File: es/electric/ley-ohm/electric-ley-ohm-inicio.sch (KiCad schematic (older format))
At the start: 60 parts

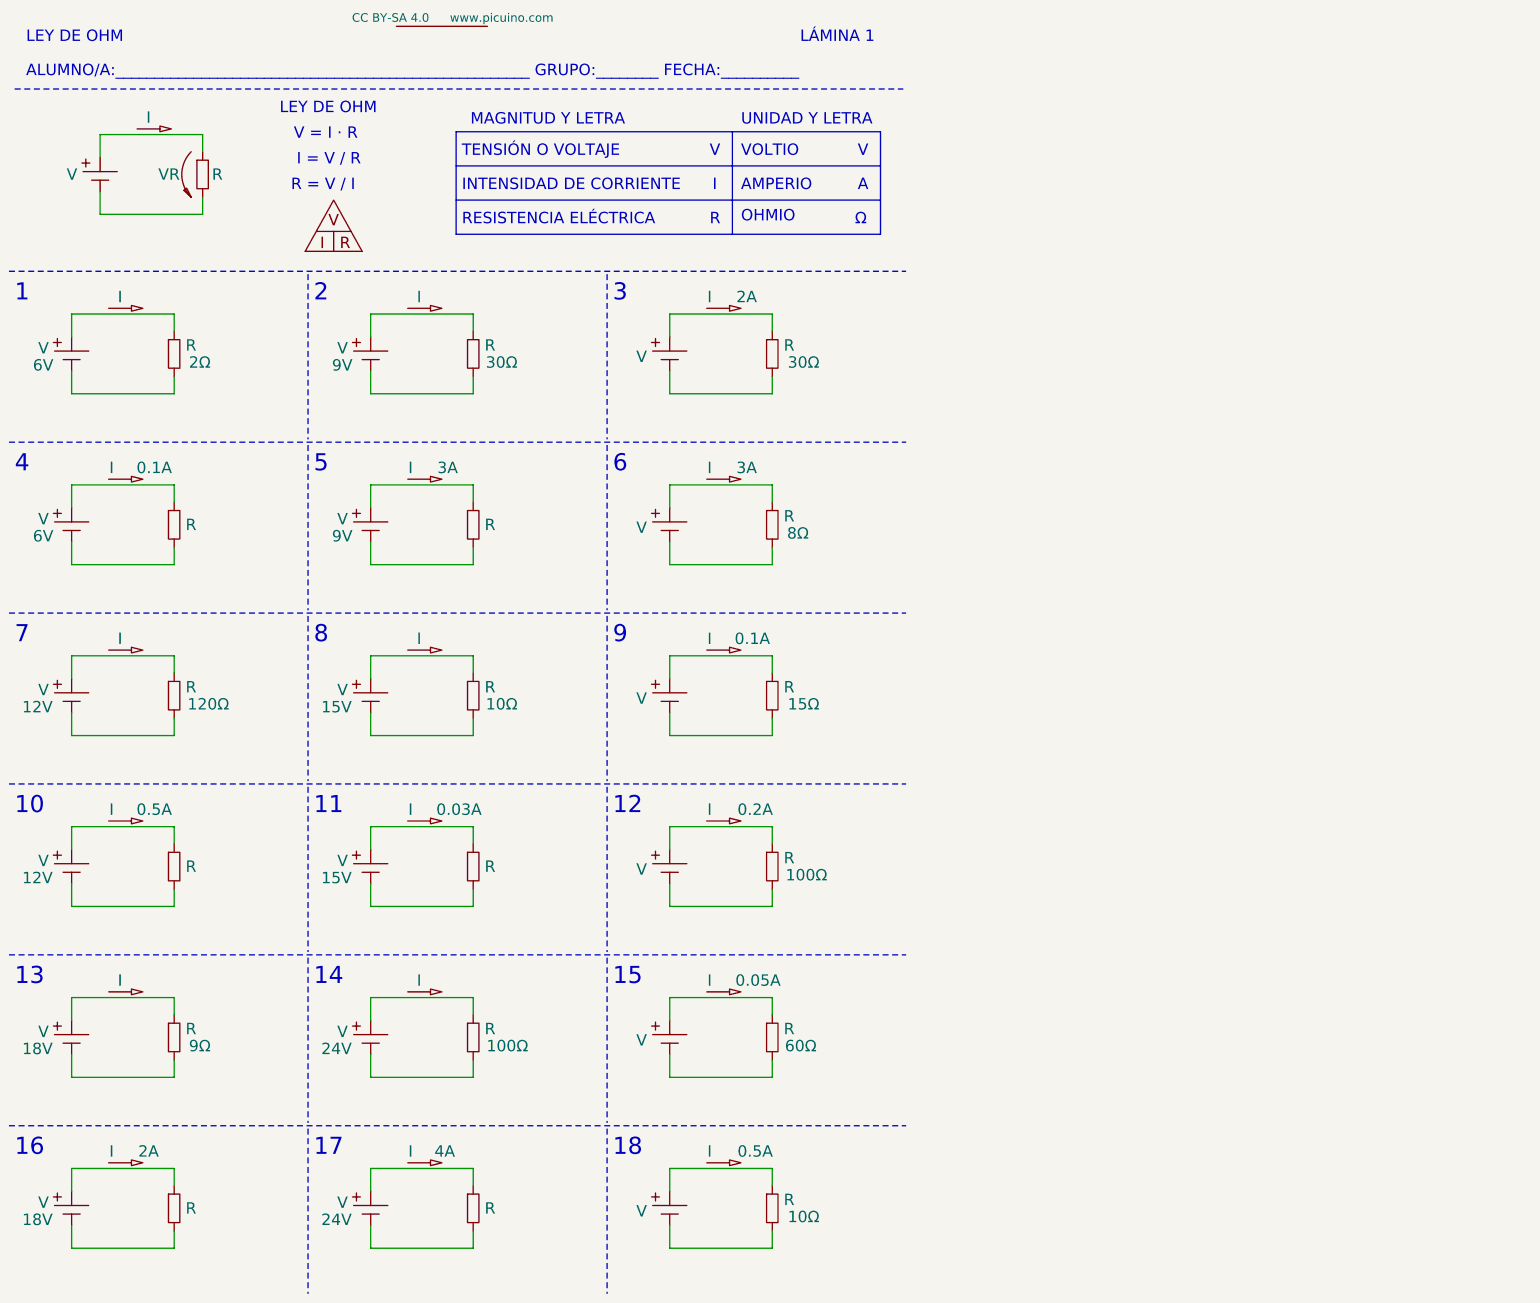
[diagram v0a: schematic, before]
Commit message: Añadida página de la ley de Ohm
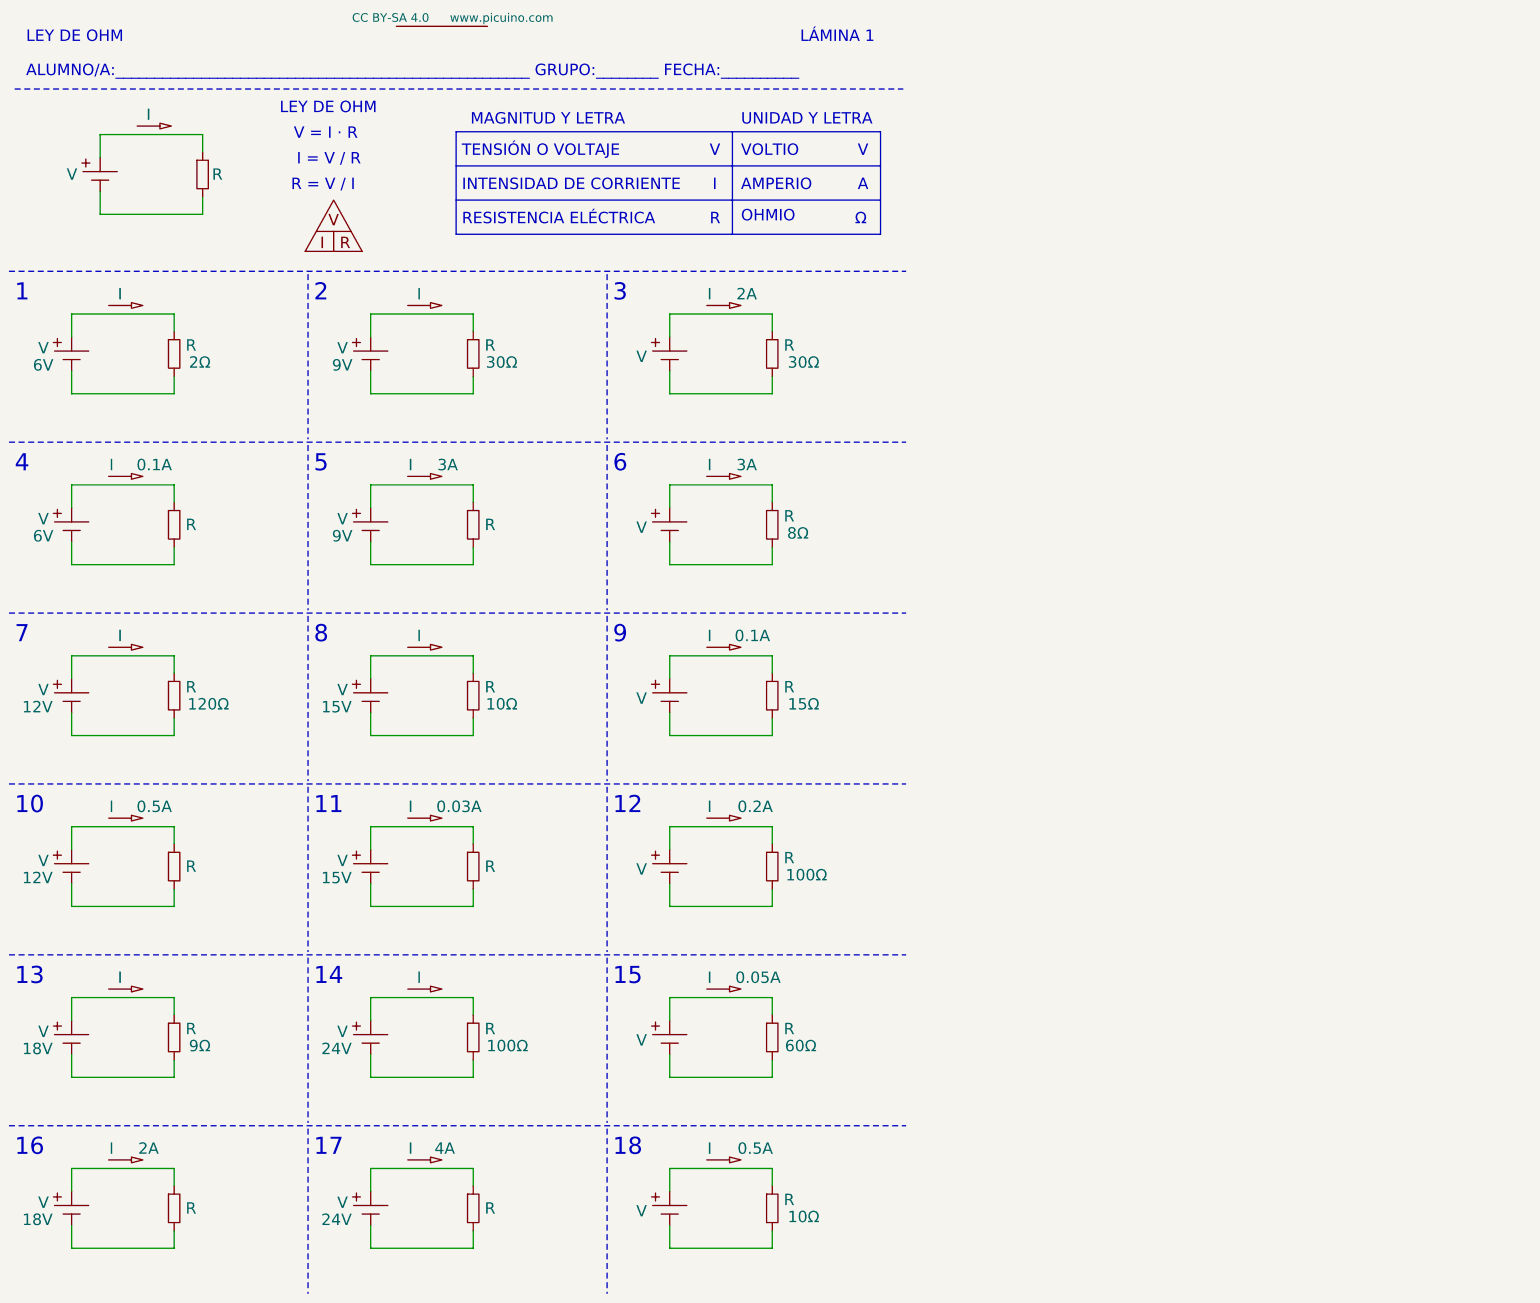
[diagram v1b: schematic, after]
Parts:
- removed VR: voltaje_drop, symbol simbolos:voltaje_drop
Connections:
- new net: R.~, V.~ (x19)
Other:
- moved on the sheet: I
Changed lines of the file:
@@
 	1900 2000 1900 1850
-$Comp
-L simbolos:voltaje_drop VR
-U 1 1 5C05123E
-P 1800 1650
-F 0 "VR" H 1700 1650 100 0000 R CNN
-F 1 "voltaje_drop" V 1800 1650 20  0001 C CNN
-F 2 "" H 1800 1650 50  0001 C CNN
-F 3 "" H 1800 1650 50  0001 C CNN
-	1    1800 1650
-	1    0    0    -1
-$EndComp
 $Comp
 L simbolos:Pila V
@@
 L simbolos:current I
 U 1 1 5C053812
-P 1325 1250
-F 0 "I" H 1425 1350 100 0000 C CNN
-F 1 "current" H 1450 1225 50  0001 C CNN
-F 2 "" H 1475 1250 50  0001 C CNN
-F 3 "" H 1475 1250 50  0001 C CNN
-	1    1325 1250
+P 1325 1225
+F 0 "I" H 1425 1325 100 0000 C CNN
+F 1 "current" H 1450 1200 50  0001 C CNN
+F 2 "" H 1475 1225 50  0001 C CNN
+F 3 "" H 1475 1225 50  0001 C CNN
+	1    1325 1225
 	1    0    0    -1
 $EndComp
@@
 L simbolos:current I
 U 1 1 60A5063B
-P 1075 2825
-F 0 "I" H 1175 2925 100 0000 C CNN
-F 1 "current" H 1200 2800 50  0001 C CNN
-F 2 "" H 1225 2825 50  0001 C CNN
-F 3 "" H 1225 2825 50  0001 C CNN
-	1    1075 2825
+P 1075 2800
+F 0 "I" H 1175 2900 100 0000 C CNN
+F 1 "current" H 1200 2775 50  0001 C CNN
+F 2 "" H 1225 2800 50  0001 C CNN
+F 3 "" H 1225 2800 50  0001 C CNN
+	1    1075 2800
 	1    0    0    -1
 $EndComp
@@
 L simbolos:current I
 U 1 1 60A5A859
-P 1075 4325
-F 0 "I" H 1100 4425 100 0000 C CNN
-F 1 "0.1A" H 1475 4425 100 0000 C CNN
-F 2 "" H 1225 4325 50  0001 C CNN
-F 3 "" H 1225 4325 50  0001 C CNN
-	1    1075 4325
+P 1075 4300
+F 0 "I" H 1100 4400 100 0000 C CNN
+F 1 "0.1A" H 1475 4400 100 0000 C CNN
+F 2 "" H 1225 4300 50  0001 C CNN
+F 3 "" H 1225 4300 50  0001 C CNN
+	1    1075 4300
 	1    0    0    -1
 $EndComp
@@
 L simbolos:current I
 U 1 1 60A5BC08
-P 1075 5825
-F 0 "I" H 1175 5925 100 0000 C CNN
-F 1 "current" H 1200 5800 50  0001 C CNN
-F 2 "" H 1225 5825 50  0001 C CNN
-F 3 "" H 1225 5825 50  0001 C CNN
-	1    1075 5825
+P 1075 5800
+F 0 "I" H 1175 5900 100 0000 C CNN
+F 1 "current" H 1200 5775 50  0001 C CNN
+F 2 "" H 1225 5800 50  0001 C CNN
+F 3 "" H 1225 5800 50  0001 C CNN
+	1    1075 5800
 	1    0    0    -1
 $EndComp
@@
 L simbolos:current I
 U 1 1 60A5E708
-P 1075 8825
-F 0 "I" H 1175 8925 100 0000 C CNN
-F 1 "current" H 1200 8800 50  0001 C CNN
-F 2 "" H 1225 8825 50  0001 C CNN
-F 3 "" H 1225 8825 50  0001 C CNN
-	1    1075 8825
+P 1075 8800
+F 0 "I" H 1175 8900 100 0000 C CNN
+F 1 "current" H 1200 8775 50  0001 C CNN
+F 2 "" H 1225 8800 50  0001 C CNN
+F 3 "" H 1225 8800 50  0001 C CNN
+	1    1075 8800
 	1    0    0    -1
 $EndComp
@@
 L simbolos:current I
 U 1 1 60A64725
-P 3700 2825
-F 0 "I" H 3800 2925 100 0000 C CNN
-F 1 "current" H 3825 2800 50  0001 C CNN
-F 2 "" H 3850 2825 50  0001 C CNN
-F 3 "" H 3850 2825 50  0001 C CNN
-	1    3700 2825
+P 3700 2800
+F 0 "I" H 3800 2900 100 0000 C CNN
+F 1 "current" H 3825 2775 50  0001 C CNN
+F 2 "" H 3850 2800 50  0001 C CNN
+F 3 "" H 3850 2800 50  0001 C CNN
+	1    3700 2800
 	1    0    0    -1
 $EndComp
@@
 L simbolos:current I
 U 1 1 60A6C8CE
-P 3700 4325
-F 0 "I" H 3725 4425 100 0000 C CNN
-F 1 "3A" H 4050 4425 100 0000 C CNN
-F 2 "" H 3850 4325 50  0001 C CNN
-F 3 "" H 3850 4325 50  0001 C CNN
-	1    3700 4325
+P 3700 4300
+F 0 "I" H 3725 4400 100 0000 C CNN
+F 1 "3A" H 4050 4400 100 0000 C CNN
+F 2 "" H 3850 4300 50  0001 C CNN
+F 3 "" H 3850 4300 50  0001 C CNN
+	1    3700 4300
 	1    0    0    -1
 $EndComp
@@
 L simbolos:current I
 U 1 1 60A6EA9F
-P 3700 5825
-F 0 "I" H 3800 5925 100 0000 C CNN
-F 1 "current" H 3825 5800 50  0001 C CNN
-F 2 "" H 3850 5825 50  0001 C CNN
-F 3 "" H 3850 5825 50  0001 C CNN
-	1    3700 5825
+P 3700 5800
+F 0 "I" H 3800 5900 100 0000 C CNN
+F 1 "current" H 3825 5775 50  0001 C CNN
+F 2 "" H 3850 5800 50  0001 C CNN
+F 3 "" H 3850 5800 50  0001 C CNN
+	1    3700 5800
 	1    0    0    -1
 $EndComp
@@
 L simbolos:current I
 U 1 1 60A72F65
-P 3700 8825
-F 0 "I" H 3800 8925 100 0000 C CNN
-F 1 "current" H 3825 8800 50  0001 C CNN
-F 2 "" H 3850 8825 50  0001 C CNN
-F 3 "" H 3850 8825 50  0001 C CNN
-	1    3700 8825
+P 3700 8800
+F 0 "I" H 3800 8900 100 0000 C CNN
+F 1 "current" H 3825 8775 50  0001 C CNN
+F 2 "" H 3850 8800 50  0001 C CNN
+F 3 "" H 3850 8800 50  0001 C CNN
+	1    3700 8800
 	1    0    0    -1
 $EndComp
@@
 L simbolos:current I
 U 1 1 60AADE55
-P 1075 7325
-F 0 "I" H 1100 7425 100 0000 C CNN
-F 1 "0.5A" H 1475 7425 100 0000 C CNN
-F 2 "" H 1225 7325 50  0001 C CNN
-F 3 "" H 1225 7325 50  0001 C CNN
-	1    1075 7325
+P 1075 7300
+F 0 "I" H 1100 7400 100 0000 C CNN
+F 1 "0.5A" H 1475 7400 100 0000 C CNN
+F 2 "" H 1225 7300 50  0001 C CNN
+F 3 "" H 1225 7300 50  0001 C CNN
+	1    1075 7300
 	1    0    0    -1
 $EndComp
@@
 L simbolos:current I
 U 1 1 60AAEB67
-P 3700 7325
-F 0 "I" H 3725 7425 100 0000 C CNN
-F 1 "0.03A" H 4150 7425 100 0000 C CNN
-F 2 "" H 3850 7325 50  0001 C CNN
-F 3 "" H 3850 7325 50  0001 C CNN
-	1    3700 7325
+P 3700 7300
+F 0 "I" H 3725 7400 100 0000 C CNN
+F 1 "0.03A" H 4150 7400 100 0000 C CNN
+F 2 "" H 3850 7300 50  0001 C CNN
+F 3 "" H 3850 7300 50  0001 C CNN
+	1    3700 7300
 	1    0    0    -1
 $EndComp
@@
 L simbolos:current I
 U 1 1 60AAFD37
-P 1075 10325
-F 0 "I" H 1100 10425 100 0000 C CNN
-F 1 "2A" H 1425 10425 100 0000 C CNN
-F 2 "" H 1225 10325 50  0001 C CNN
-F 3 "" H 1225 10325 50  0001 C CNN
-	1    1075 10325
+P 1075 10300
+F 0 "I" H 1100 10400 100 0000 C CNN
+F 1 "2A" H 1425 10400 100 0000 C CNN
+F 2 "" H 1225 10300 50  0001 C CNN
+F 3 "" H 1225 10300 50  0001 C CNN
+	1    1075 10300
 	1    0    0    -1
 $EndComp
@@
 L simbolos:current I
 U 1 1 60AB00CA
-P 3700 10325
-F 0 "I" H 3725 10425 100 0000 C CNN
-F 1 "4A" H 4025 10425 100 0000 C CNN
-F 2 "" H 3850 10325 50  0001 C CNN
-F 3 "" H 3850 10325 50  0001 C CNN
-	1    3700 10325
+P 3700 10300
+F 0 "I" H 3725 10400 100 0000 C CNN
+F 1 "4A" H 4025 10400 100 0000 C CNN
+F 2 "" H 3850 10300 50  0001 C CNN
+F 3 "" H 3850 10300 50  0001 C CNN
+	1    3700 10300
 	1    0    0    -1
 $EndComp
@@
 L simbolos:current I
 U 1 1 60AB3649
-P 6325 2825
-F 0 "I" H 6350 2925 100 0000 C CNN
-F 1 "2A" H 6675 2925 100 0000 C CNN
-F 2 "" H 6475 2825 50  0001 C CNN
-F 3 "" H 6475 2825 50  0001 C CNN
-	1    6325 2825
+P 6325 2800
+F 0 "I" H 6350 2900 100 0000 C CNN
+F 1 "2A" H 6675 2900 100 0000 C CNN
+F 2 "" H 6475 2800 50  0001 C CNN
+F 3 "" H 6475 2800 50  0001 C CNN
+	1    6325 2800
 	1    0    0    -1
 $EndComp
@@
 L simbolos:current I
 U 1 1 60AB39D5
-P 6325 4325
-F 0 "I" H 6350 4425 100 0000 C CNN
-F 1 "3A" H 6675 4425 100 0000 C CNN
-F 2 "" H 6475 4325 50  0001 C CNN
-F 3 "" H 6475 4325 50  0001 C CNN
-	1    6325 4325
+P 6325 4300
+F 0 "I" H 6350 4400 100 0000 C CNN
+F 1 "3A" H 6675 4400 100 0000 C CNN
+F 2 "" H 6475 4300 50  0001 C CNN
+F 3 "" H 6475 4300 50  0001 C CNN
+	1    6325 4300
 	1    0    0    -1
 $EndComp
@@
 L simbolos:current I
 U 1 1 60AB3D32
-P 6325 5825
-F 0 "I" H 6350 5925 100 0000 C CNN
-F 1 "0.1A" H 6725 5925 100 0000 C CNN
-F 2 "" H 6475 5825 50  0001 C CNN
-F 3 "" H 6475 5825 50  0001 C CNN
-	1    6325 5825
+P 6325 5800
+F 0 "I" H 6350 5900 100 0000 C CNN
+F 1 "0.1A" H 6725 5900 100 0000 C CNN
+F 2 "" H 6475 5800 50  0001 C CNN
+F 3 "" H 6475 5800 50  0001 C CNN
+	1    6325 5800
 	1    0    0    -1
 $EndComp
@@
 L simbolos:current I
 U 1 1 60AB4131
-P 6325 7325
-F 0 "I" H 6350 7425 100 0000 C CNN
-F 1 "0.2A" H 6750 7425 100 0000 C CNN
-F 2 "" H 6475 7325 50  0001 C CNN
-F 3 "" H 6475 7325 50  0001 C CNN
-	1    6325 7325
+P 6325 7300
+F 0 "I" H 6350 7400 100 0000 C CNN
+F 1 "0.2A" H 6750 7400 100 0000 C CNN
+F 2 "" H 6475 7300 50  0001 C CNN
+F 3 "" H 6475 7300 50  0001 C CNN
+	1    6325 7300
 	1    0    0    -1
 $EndComp
@@
 L simbolos:current I
 U 1 1 60AB44F6
-P 6325 8825
-F 0 "I" H 6350 8925 100 0000 C CNN
-F 1 "0.05A" H 6775 8925 100 0000 C CNN
-F 2 "" H 6475 8825 50  0001 C CNN
-F 3 "" H 6475 8825 50  0001 C CNN
-	1    6325 8825
+P 6325 8800
+F 0 "I" H 6350 8900 100 0000 C CNN
+F 1 "0.05A" H 6775 8900 100 0000 C CNN
+F 2 "" H 6475 8800 50  0001 C CNN
+F 3 "" H 6475 8800 50  0001 C CNN
+	1    6325 8800
 	1    0    0    -1
 $EndComp
@@
 L simbolos:current I
 U 1 1 60AB4A8B
-P 6325 10325
-F 0 "I" H 6350 10425 100 0000 C CNN
-F 1 "0.5A" H 6750 10425 100 0000 C CNN
-F 2 "" H 6475 10325 50  0001 C CNN
-F 3 "" H 6475 10325 50  0001 C CNN
-	1    6325 10325
-	1    0    0    -1
-$EndComp
+P 6325 10300
+F 0 "I" H 6350 10400 100 0000 C CNN
+F 1 "0.5A" H 6750 10400 100 0000 C CNN
+F 2 "" H 6475 10300 50  0001 C CNN
+F 3 "" H 6475 10300 50  0001 C CNN
+	1    6325 10300
+	1    0    0    -1
+$EndComp

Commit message: Cambios a 23/05/2022.
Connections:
- new net: R.~, V.~ (x19)
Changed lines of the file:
@@
 $Descr A4 8268 11693 portrait
 encoding utf-8
-Sheet 1 1
+Sheet 1 2
 Title "Ley de Ohm"
 Date "2021-05-15"
@@
 Text Notes 5500 10275 0    150  ~ 0
 18
+$Sheet
+S 10000 750  2500 1725
+U 628BB5D7
+F0 "Ley de Ohm 2" 100
+F1 "electric-ley-ohm-inicio-02.sch" 100
+$EndSheet
 $EndSCHEMATC
